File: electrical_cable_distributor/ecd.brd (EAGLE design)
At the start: 4 parts, among them X1 DG300-5.0-03P-13-00AH, X2 DG300-5.0-03P-13-00AH, X3 DG300-5.0-03P-13-00AH, X4 DG300-5.0-03P-13-00AH

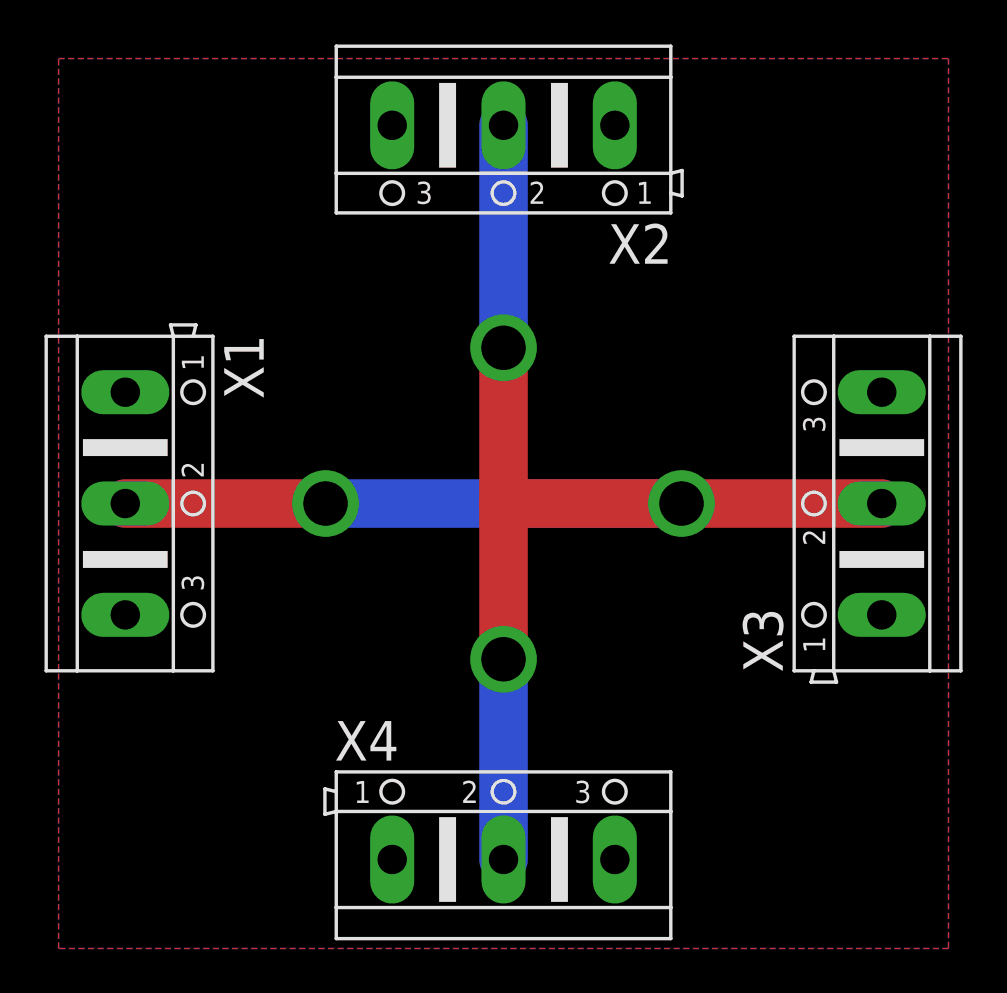
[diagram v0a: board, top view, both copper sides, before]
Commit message: new design, with brick closer to each other
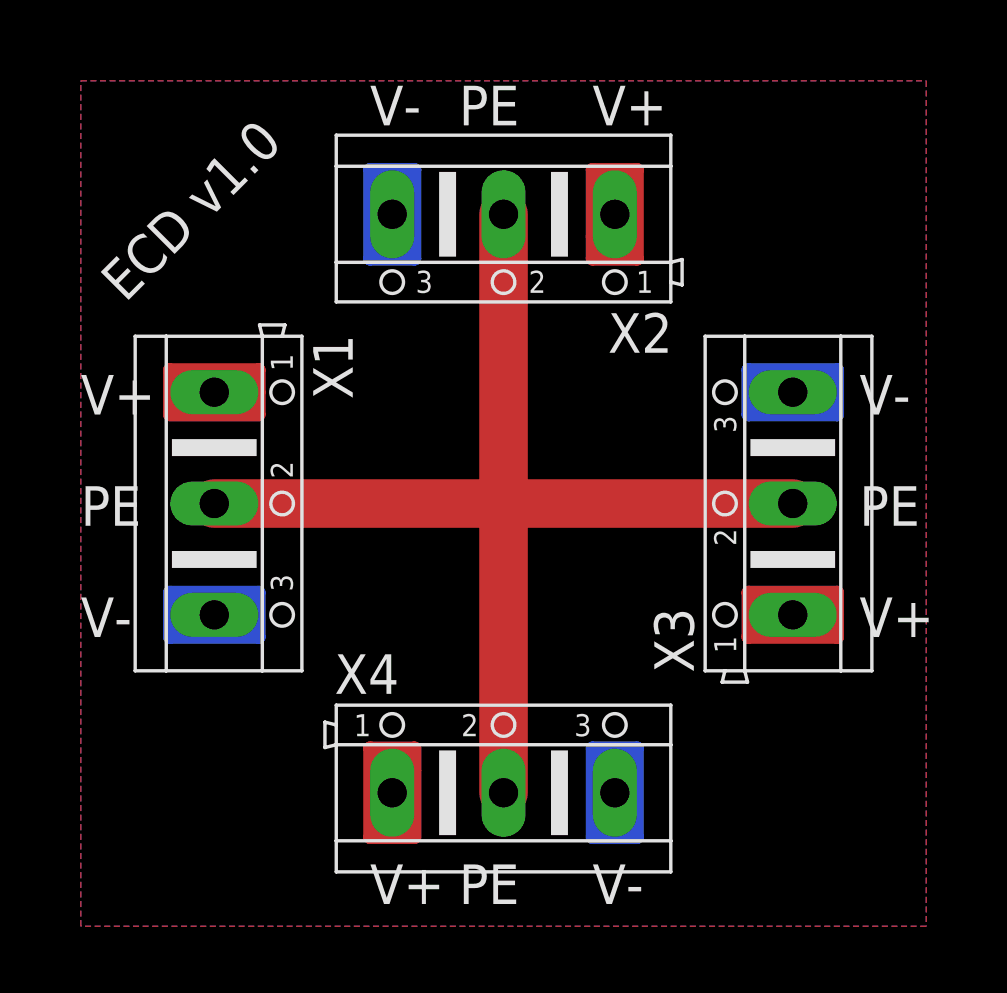
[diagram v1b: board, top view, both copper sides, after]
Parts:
- X1, X2, X3, X4: value DG300-5.0-03P-13-00AH -> (none)
- moved X1 4.00 mm to (30.0, 42.0)
- moved X2 4.00 mm to (43.0, 55.0)
- moved X3 4.00 mm to (56.0, 42.0)
- moved X4 3.00 mm to (43.0, 29.0)
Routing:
- net V-: track 0.00 -> 62.8 mm
- net V+: track 0.00 -> 54.8 mm
- net PE: track 75.0 -> 52.0 mm, vias 4 -> 0
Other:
- board text added: "ECD v1.0"
- board text added: "PE"
- board text added: "V+"
- board text added: "V-"
